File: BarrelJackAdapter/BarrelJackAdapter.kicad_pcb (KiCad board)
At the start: 2 copper layers, 15.2 x 45.6 mm, 7 parts, among them J1 Barrel_Jack_Switch, J2 Conn_01x03, J4 Conn_01x03, U1 L7805

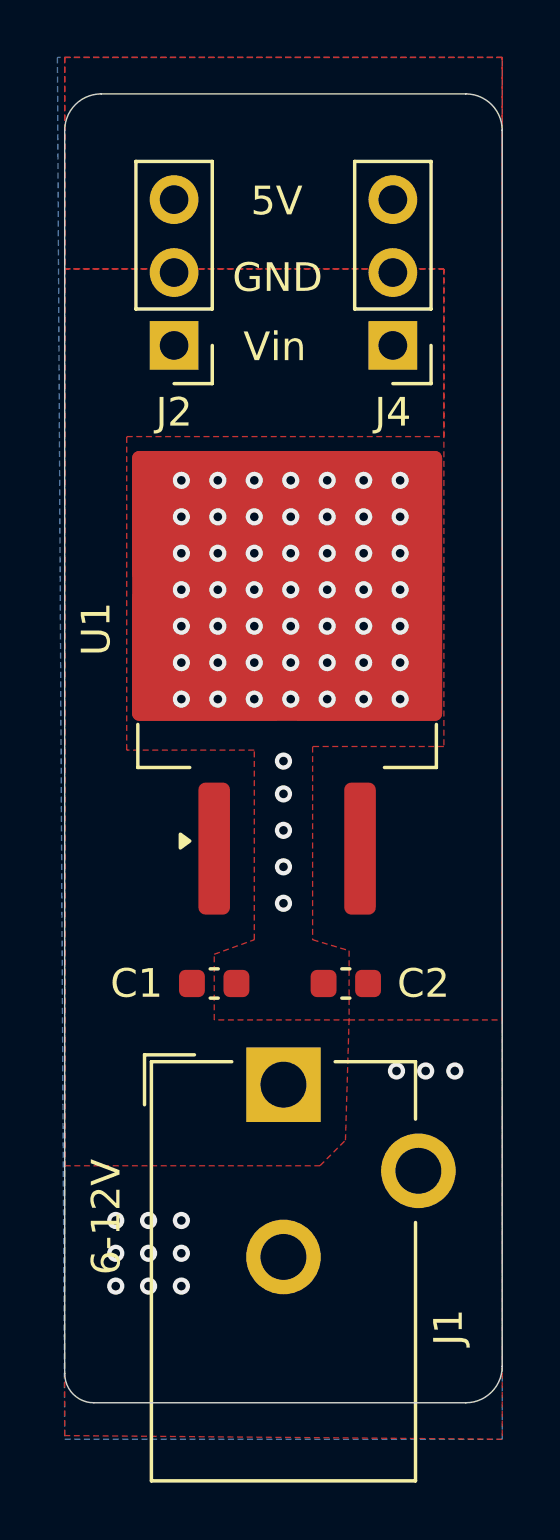
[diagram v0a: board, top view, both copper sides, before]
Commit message: add some silkscreen
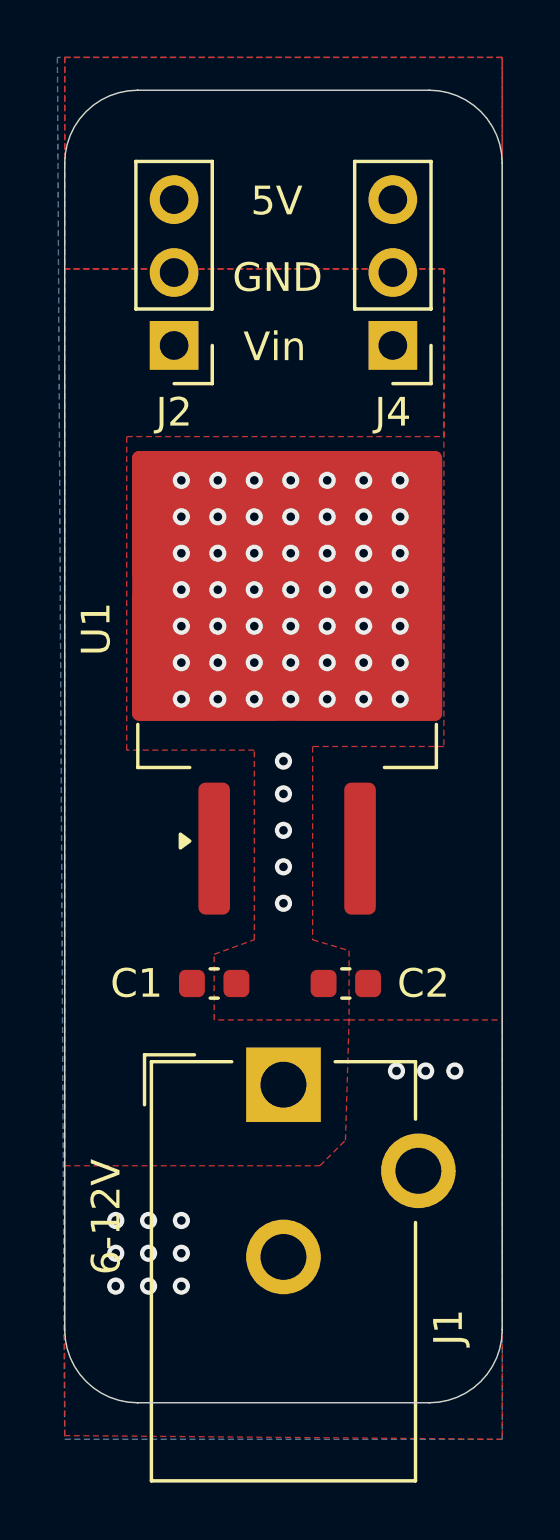
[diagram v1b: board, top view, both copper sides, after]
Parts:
- moved G*** 8.51 mm to (185.4, 49.5)
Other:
- board size 15.2 x 45.6 mm -> 15.2 x 45.7 mm
- board text added: "Barrel Jack Adapter. Copyright 2024 Tad Truex"
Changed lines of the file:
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@@
 		(31 "B.Cu" signal)
 		(32 "B.Adhes" user "B.Adhesive")
-		(33 "F.Adhes" user "F.Adhesive")
 		(34 "B.Paste" user)
 		(35 "F.Paste" user)
@@
 		(38 "B.Mask" user)
 		(39 "F.Mask" user)
-		(40 "Dwgs.User" user "User.Drawings")
-		(41 "Cmts.User" user "User.Comments")
-		(42 "Eco1.User" user "User.Eco1")
-		(43 "Eco2.User" user "User.Eco2")
 		(44 "Edge.Cuts" user)
 		(45 "Margin" user)
@@
 		(48 "B.Fab" user)
 		(49 "F.Fab" user)
-		(50 "User.1" user)
-		(51 "User.2" user)
-		(52 "User.3" user)
-		(53 "User.4" user)
-		(54 "User.5" user)
-		(55 "User.6" user)
-		(56 "User.7" user)
-		(57 "User.8" user)
-		(58 "User.9" user)
 	)
 	(setup
@@
 	(footprint "QRCodes:BarrelJack"
 		(layer "B.Cu")
-		(at 185.674 58.039 180)
+		(at 185.42 49.53 180)
 		(property "Reference" "G***"
 			(at 0 0 0)
@@
 		)
 	)
-	(gr_arc
-		(start 178.816 80.01)
-		(mid 178.09758 79.71242)
-		(end 177.8 78.994)
+	(gr_line
+		(start 193.04 77.47)
+		(end 193.04 36.83)
 		(stroke
 			(width 0.05)
@@
 	)
 	(gr_arc
-		(start 193.04 78.74)
-		(mid 192.668026 79.638026)
-		(end 191.77 80.01)
+		(start 177.8 36.83)
+		(mid 178.543949 35.033949)
+		(end 180.34 34.29)
 		(stroke
 			(width 0.05)
@@
 	)
 	(gr_arc
-		(start 191.77 34.417)
-		(mid 192.668026 34.788974)
-		(end 193.04 35.687)
+		(start 193.04 77.47)
+		(mid 192.296051 79.266051)
+		(end 190.5 80.01)
 		(stroke
 			(width 0.05)
@@
 		(layer "Edge.Cuts")
 	)
-	(gr_line
-		(start 193.04 35.687)
-		(end 193.04 78.74)
+	(gr_arc
+		(start 180.34 80.01)
+		(mid 178.543949 79.266051)
+		(end 177.8 77.47)
 		(stroke
 			(width 0.05)
@@
 		(layer "Edge.Cuts")
 	)
-	(gr_line
-		(start 191.77 80.01)
-		(end 178.816 80.01)
+	(gr_arc
+		(start 190.5 34.29)
+		(mid 192.296051 35.033949)
+		(end 193.04 36.83)
 		(stroke
 			(width 0.05)
@@
 	)
 	(gr_line
-		(start 179.07 34.417)
-		(end 191.77 34.417)
+		(start 180.34 80.01)
+		(end 190.5 80.01)
 		(stroke
 			(width 0.05)
@@
 	)
 	(gr_line
-		(start 177.8 78.994)
-		(end 177.8 35.687)
+		(start 177.8 77.47)
+		(end 177.8 36.83)
 		(stroke
 			(width 0.05)
@@
 		(layer "Edge.Cuts")
 	)
-	(gr_arc
-		(start 177.8 35.687)
-		(mid 178.171974 34.788974)
-		(end 179.07 34.417)
+	(gr_line
+		(start 180.34 34.29)
+		(end 190.5 34.29)
 		(stroke
 			(width 0.05)
@@
 		(layer "Edge.Cuts")
 	)
+	(gr_text "Barrel Jack Adapter.\nCopyright 2024 Tad Truex"
+		(at 180.34 77.47 -90)
+		(layer "B.SilkS")
+		(effects
+			(font
+				(size 1 1)
+				(thickness 0.15)
+			)
+			(justify left bottom mirror)
+		)
+	)
 	(gr_text "Vin"
